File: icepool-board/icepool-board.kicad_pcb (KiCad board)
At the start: 4 copper layers, 100 x 40 mm, 120 parts, among them J1 PWR, J2 PWR_IN, J3 I2C, J4 SWD, J5 8P8C_Shielded, J6 8P8C_Shielded, SW1 B3U-1000P, U1 LD1117S33CTR, U2 LD1117S12CTR, U3 ATSAMD21E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

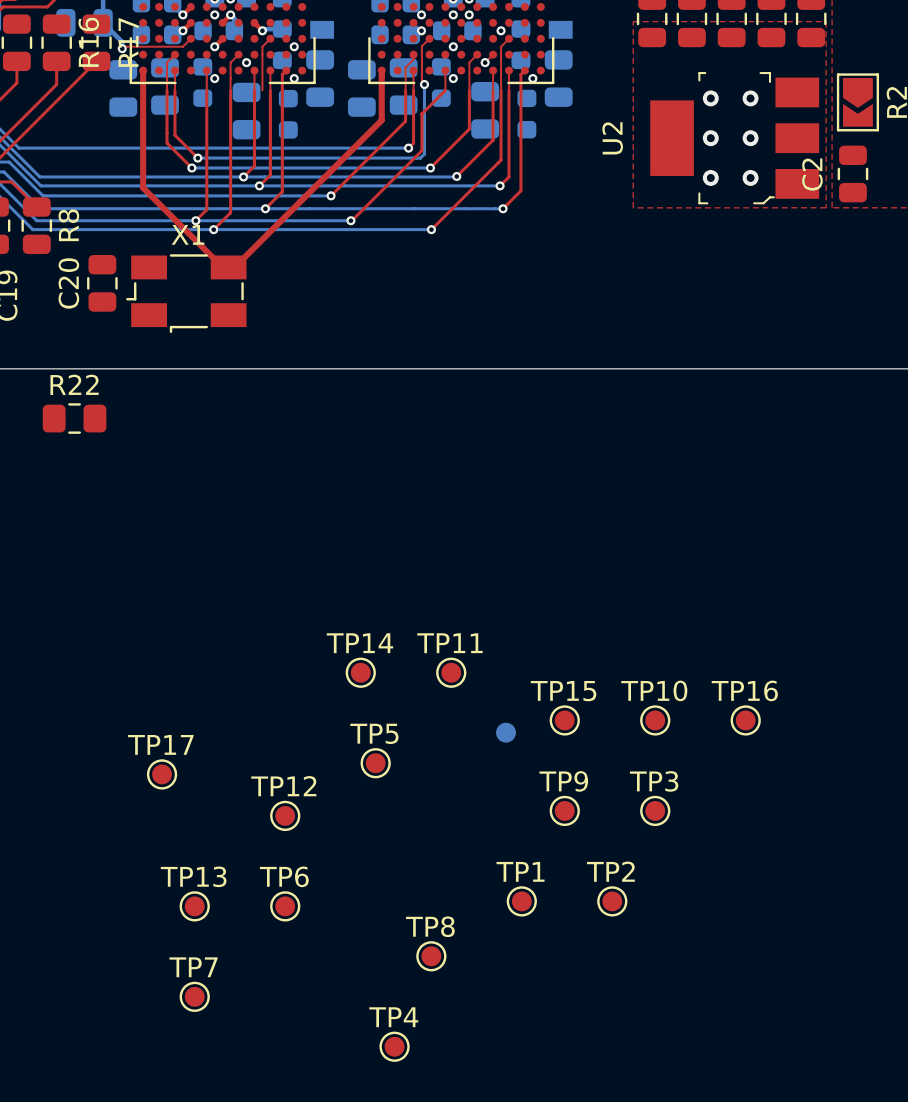
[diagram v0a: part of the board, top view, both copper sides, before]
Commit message: Removed test points. Removing soldermask instead.
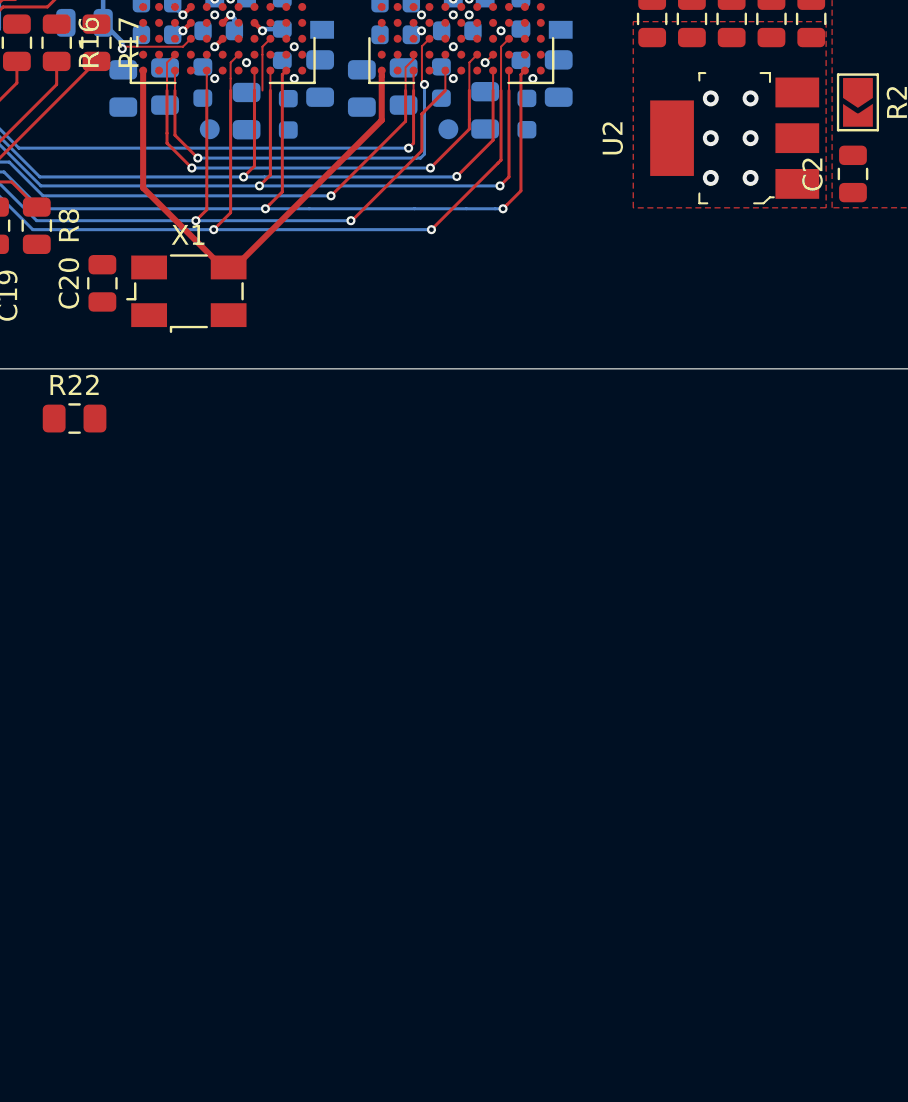
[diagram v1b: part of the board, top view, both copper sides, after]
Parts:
- removed TP1, TP10, TP11, TP12, TP13, TP14, TP15, TP16, TP2, TP3, TP4, TP5, TP6, TP7, TP8, TP9: TestPoint, TestPoint:TestPoint_Pad_D1.0mm
- TP17: moved to B.Cu
- moved TP17 32.5 mm to (70.9, 108.0), turned to 180 degrees
- moved TP18 30.5 mm to (82.9, 108.0)

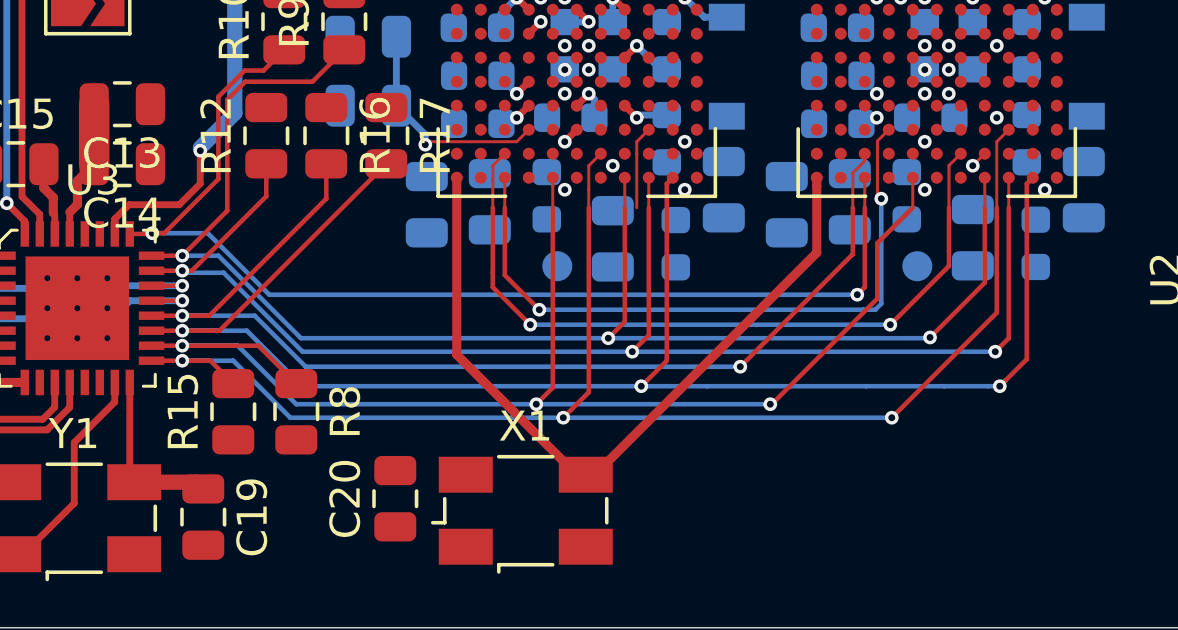
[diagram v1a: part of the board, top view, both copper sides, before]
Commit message: Opting to probe exposed pins. 0.5mm too small.
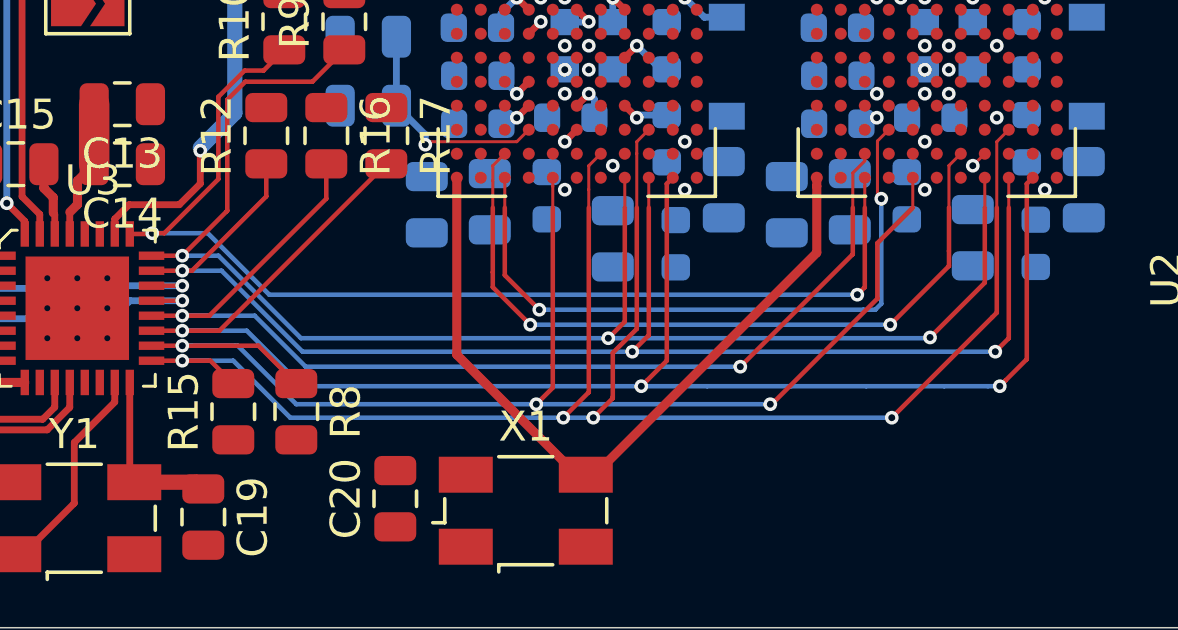
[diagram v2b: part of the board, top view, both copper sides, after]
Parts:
- removed TP17, TP18: TestPoint, TestPoint:TestPoint_Pad_D1.0mm
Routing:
- net /MOSI: track 50.8 -> 58.4 mm, vias 3 -> 4
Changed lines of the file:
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@@
     (thickness 1.6)
     (drawings 4)
-    (tracks 456)
+    (tracks 463)
     (zones 0)
-    (modules 104)
+    (modules 102)
     (nets 247)
   )
@@
     (36 B.SilkS user hide)
     (37 F.SilkS user hide)
-    (38 B.Mask user hide)
+    (38 B.Mask user)
     (39 F.Mask user)
     (40 Dwgs.User user hide)
@@
     )
   )
-  (module TestPoint:TestPoint_Pad_D1.0mm (layer B.Cu)
-    (at 82.9 107.95)
-    (descr "SMD pad as test Point, diameter 1.0mm")
-    (tags "test point SMD pad")
-    (attr virtual)
-    (fp_text reference TP18 (at 0 1.448) (layer B.SilkS)
-      (effects (font (size 1 1) (thickness 0.15)) (justify mirror))
-    )
-    (fp_text value TestPoint (at 0 -1.55) (layer B.Fab)
-      (effects (font (size 1 1) (thickness 0.15)) (justify mirror))
-    )
-    (fp_circle (center 0 0) (end 0 -0.7) (layer B.SilkS) (width 0.12))
-    (fp_circle (center 0 0) (end 1 0) (layer B.CrtYd) (width 0.05))
-    (fp_text user %R (at 0 1.45) (layer B.Fab)
-      (effects (font (size 1 1) (thickness 0.15)) (justify mirror))
-    )
-    (pad 1 smd circle (at 0 0) (size 1 1) (layers B.Cu B.Mask)
-      (net 39 /ICE40HX8K-BG121_1/CDONE))
-  )
-  (module TestPoint:TestPoint_Pad_D1.0mm (layer B.Cu)
-    (at 70.9 107.95 180)
-    (descr "SMD pad as test Point, diameter 1.0mm")
-    (tags "test point SMD pad")
-    (attr virtual)
-    (fp_text reference TP17 (at 0 1.448) (layer B.SilkS)
-      (effects (font (size 1 1) (thickness 0.15)) (justify mirror))
-    )
-    (fp_text value TestPoint (at 0 -1.55) (layer B.Fab)
-      (effects (font (size 1 1) (thickness 0.15)) (justify mirror))
-    )
-    (fp_circle (center 0 0) (end 0 -0.7) (layer B.SilkS) (width 0.12))
-    (fp_circle (center 0 0) (end 1 0) (layer B.CrtYd) (width 0.05))
-    (fp_text user %R (at 0 1.45) (layer B.Fab)
-      (effects (font (size 1 1) (thickness 0.15)) (justify mirror))
-    )
-    (pad 1 smd circle (at 0 0 180) (size 1 1) (layers B.Cu B.Mask)
-      (net 38 /ICE40HX8K-BG121_0/CDONE))
-  )
   (module Resistor_SMD:R_0805_2012Metric (layer B.Cu)
     (at 78.55 105.9 270)
@@
   (via (at 85.5 110.8) (size 0.4572) (drill 0.2286) (layers F.Cu B.Cu) (net 34))
   (segment (start 58.468199 108.168199) (end 58.4 108.1) (width 0.1524) (layer B.Cu) (net 34))
-  (segment (start 59.77791 108.168199) (end 58.468199 108.168199) (width 0.1524) (layer B.Cu) (net 34))
-  (segment (start 85.5 110.8) (end 62.409711 110.8) (width 0.1524) (layer B.Cu) (net 34))
-  (segment (start 62.409711 110.8) (end 59.77791 108.168199) (width 0.1524) (layer B.Cu) (net 34))
+  (segment (start 62.409711 110.8) (end 85.5 110.8) (width 0.1524) (layer B.Cu) (net 34))
+  (segment (start 58.4 108.1) (end 59.709711 108.1) (width 0.1524) (layer B.Cu) (net 34))
+  (segment (start 59.709711 108.1) (end 62.409711 110.8) (width 0.1524) (layer B.Cu) (net 34))
   (segment (start 73.95 103.4) (end 73.55 103.8) (width 0.1016) (layer F.Cu) (net 35))
   (segment (start 73.55 103.8) (end 73.55 104.2) (width 0.1016) (layer F.Cu) (net 35))
@@
   (segment (start 71.1 113) (end 71.1 113) (width 0.1524) (layer F.Cu) (net 35))
   (via (at 71.1 113) (size 0.4572) (drill 0.2286) (layers F.Cu B.Cu) (net 35))
+  (segment (start 73.55 110.039066) (end 72.75 110.839066) (width 0.1524) (layer F.Cu) (net 35))
+  (segment (start 73.55 106) (end 73.55 110.039066) (width 0.1524) (layer F.Cu) (net 35))
+  (segment (start 72.75 110.839066) (end 72.75 112.3) (width 0.1524) (layer F.Cu) (net 35))
+  (segment (start 72.75 112.3) (end 72.75 112.35) (width 0.1524) (layer F.Cu) (net 35))
+  (segment (start 72.75 112.35) (end 72.1 113) (width 0.1524) (layer F.Cu) (net 35))
+  (segment (start 72.1 113) (end 72.1 113) (width 0.1524) (layer F.Cu) (net 35))
+  (via (at 72.1 113) (size 0.4572) (drill 0.2286) (layers F.Cu B.Cu) (net 35))
   (segment (start 59.6375 110.1) (end 58.4 110.1) (width 0.1524) (layer F.Cu) (net 36))
   (segment (start 65.2 104.5375) (end 59.6375 110.1) (width 0.1524) (layer F.Cu) (net 36))

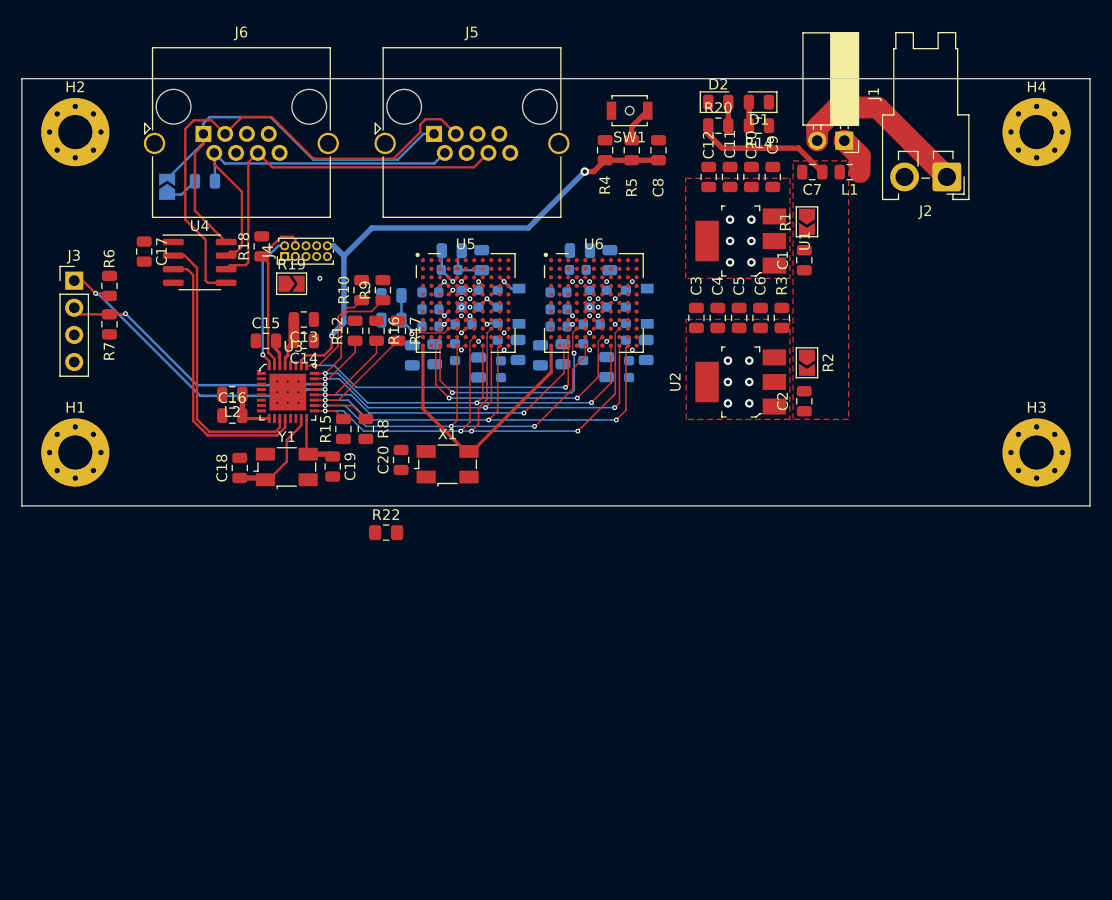
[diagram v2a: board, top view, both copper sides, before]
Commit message: Power planes and lines placed.
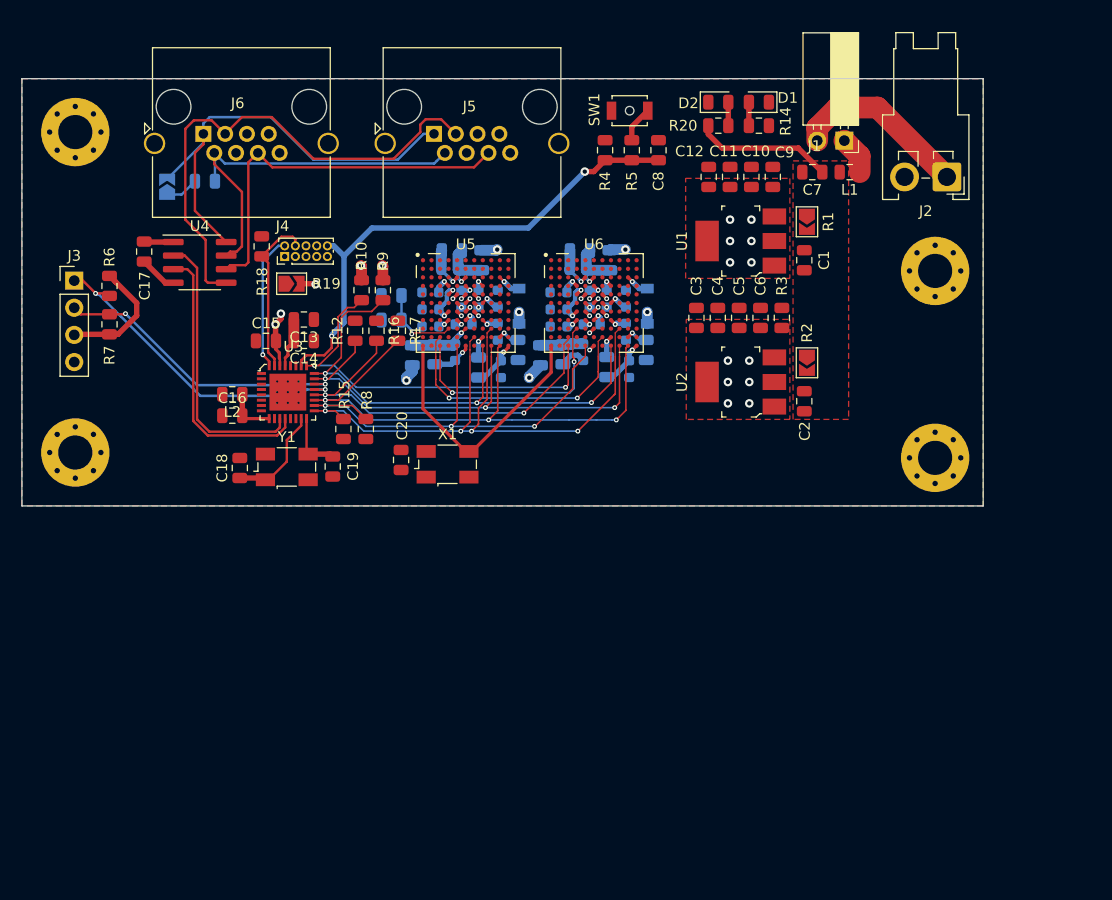
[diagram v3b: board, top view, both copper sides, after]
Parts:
- removed R22: OMIT, Resistor_SMD:R_0805_2012Metric_Pad1.15x1.40mm_HandSolder
- moved H4 31.9 mm to (115.5, 115.5)
- moved H3 19.5 mm to (115.5, 98.0)
- turned C37 to 0 degrees
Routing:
- net +1V2: track 5.92 -> 107.6 mm, vias 10 -> 18
- net +3V3: track 9.30 -> 52.6 mm, vias 11 -> 25
- net GND: track 0.00 -> 15.7 mm, vias 11 -> 20
- net /ICE40HX8K-BG121_1/VCCPLL1: track 0.00 -> 5.97 mm
- net /ICE40HX8K-BG121_0/VCCPLL0: track 0.57 -> 6.10 mm
- net /ICE40HX8K-BG121_1/VCCPLL0: track 0.00 -> 4.60 mm
- net /ICE40HX8K-BG121_1/GNDPLL1: track 0.00 -> 3.94 mm
- net /ICE40HX8K-BG121_0/GNDPLL0: track 0.21 -> 4.06 mm
- net /ICE40HX8K-BG121_1/GNDPLL0: track 0.00 -> 3.08 mm
- net /ICE40HX8K-BG121_1/VPP_2V5: track 0.00 -> 2.23 mm
- net /ICE40HX8K-BG121_1/SPI_SS_B: track 0.00 -> 2.14 mm, vias 0 -> 1
- net /ICE40HX8K-BG121_0/SPI_SS_B: track 0.00 -> 2.14 mm, vias 0 -> 1
- net /ICE40HX8K-BG121_0/CDONE: track 0.00 -> 2.07 mm
- net /ICE40HX8K-BG121_0/VCCPLL1: track 4.74 -> 6.46 mm
- net /ICE40HX8K-BG121_1/CDONE: track 0.57 -> 2.03 mm
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- added copper zone on In1.Cu, net +1V2
- added copper zone on In1.Cu, net +3V3
- added copper zone on B.Cu, net GND
- added copper zone on F.Cu, net GND
- added copper zone on In2.Cu, net GND
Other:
- board size 100 x 40 mm -> 90 x 40 mm

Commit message: Final touches. Ran DRC. Some things need tweaking.
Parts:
- moved R12 0.90 mm to (61.2, 104.5)
- moved C33 0.15 mm to (74.7, 107.2)
- moved C46 0.15 mm to (86.7, 107.2)
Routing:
- net GND: track 15.7 -> 47.8 mm, vias 20 -> 61
- net +3V3: track 52.6 -> 70.9 mm, vias 25 -> 36
- net +1V2: track 107.6 -> 95.0 mm
- net Net-(R1-Pad1): track 0.00 -> 3.14 mm
- net Net-(R2-Pad1): track 0.00 -> 3.14 mm
- net Net-(J4-Pad1): track 0.00 -> 2.58 mm
- net /ICE40HX8K-BG121_1/VCCPLL0: track 4.60 -> 5.86 mm
- net /ICE40HX8K-BG121_1/GNDPLL0: track 3.08 -> 4.28 mm

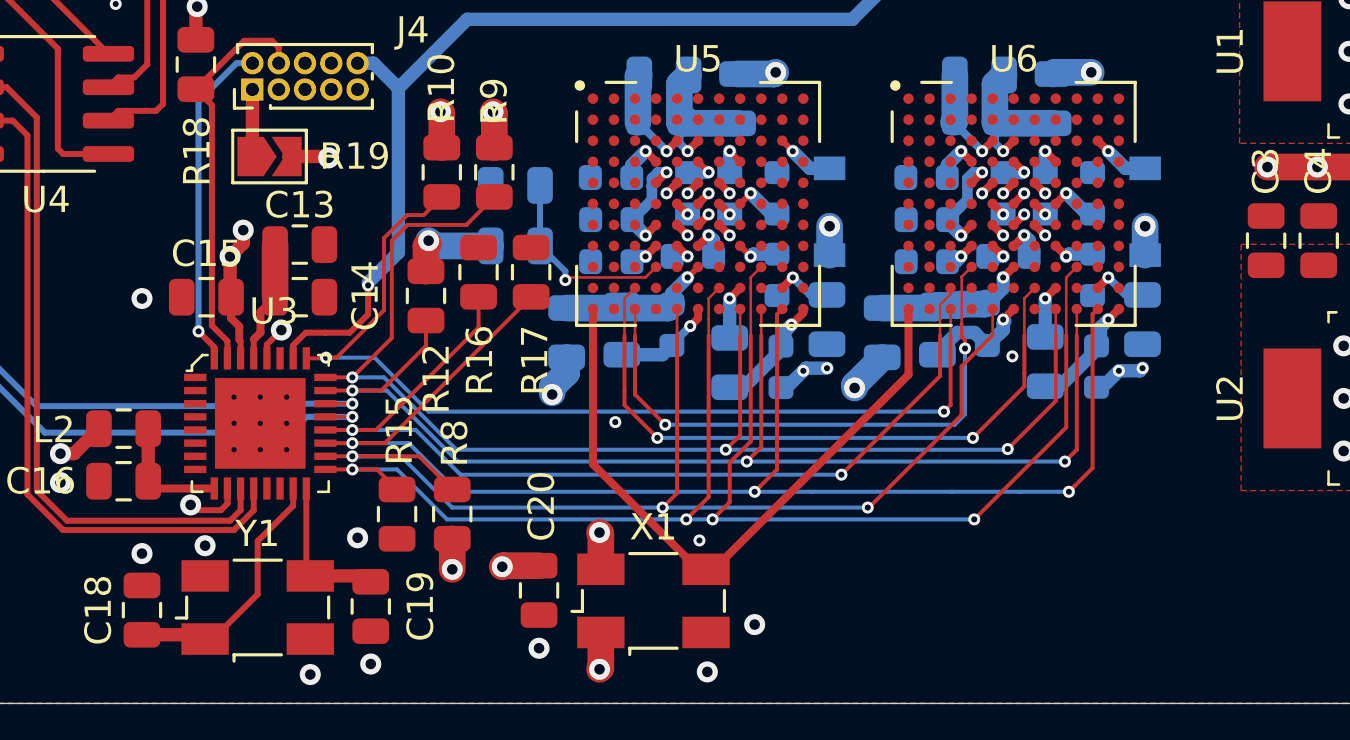
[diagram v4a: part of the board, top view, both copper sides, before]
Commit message: Took on DRC.
Two errors remain: two vias within blonde one of 5 mil, probably OK?
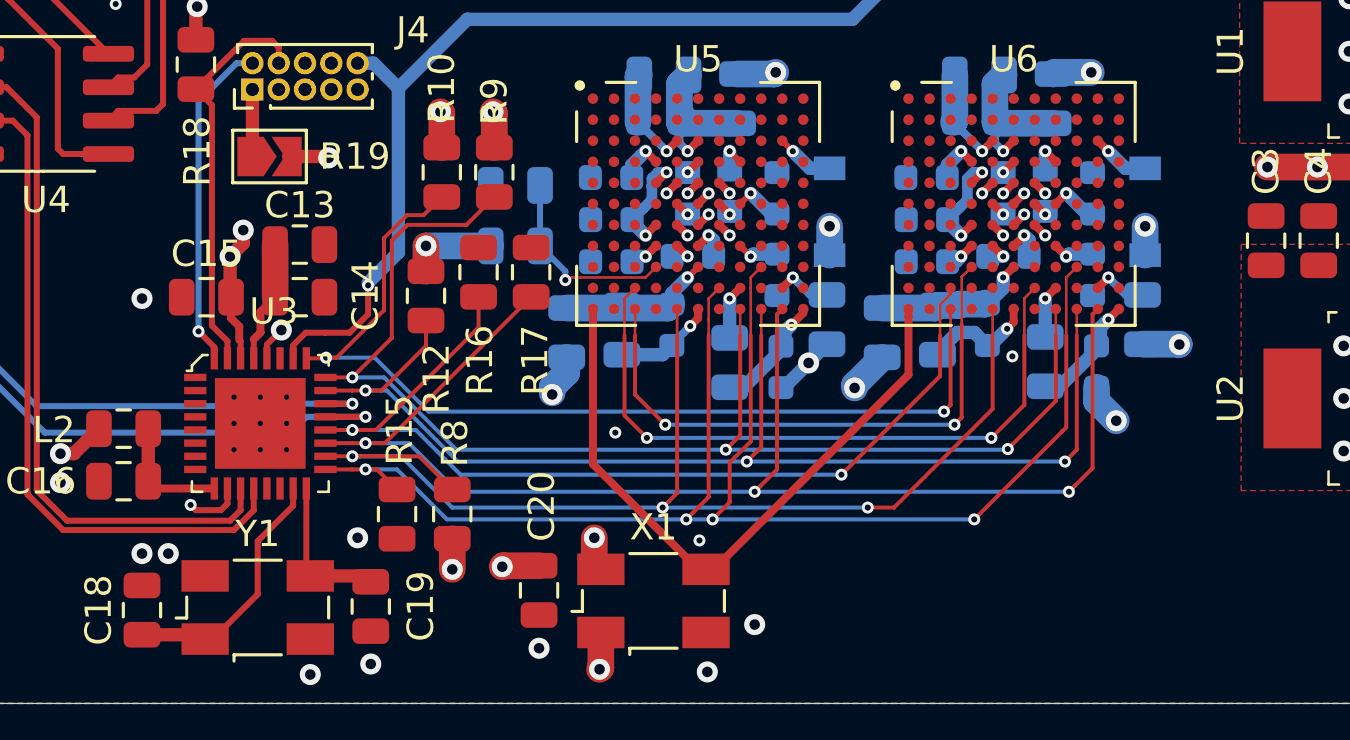
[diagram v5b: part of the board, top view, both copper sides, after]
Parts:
- moved C27 0.10 mm to (72.8, 100.5)
- moved C40 0.10 mm to (84.8, 100.5)
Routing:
- net GND: track 47.8 -> 49.8 mm, vias 61 -> 60
- net +3V3: track 70.9 -> 69.1 mm
- net /SDA: track 30.6 -> 31.6 mm
- net /FIFO_0_1: track 25.1 -> 25.7 mm
- net /~WE: track 43.4 -> 44.0 mm
- net /CRESET_B: track 45.8 -> 45.2 mm
- net /SCK: track 52.9 -> 52.4 mm
- net /MOSI: track 58.4 -> 57.9 mm
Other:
- rule via_min_size: 0.45 -> 0.2
